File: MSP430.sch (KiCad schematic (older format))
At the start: 23 parts, among them P1 CONN_02X07, SW1 2M1-SP1-T2-B4-M6RE, U6 MSP430F2274TRHAR

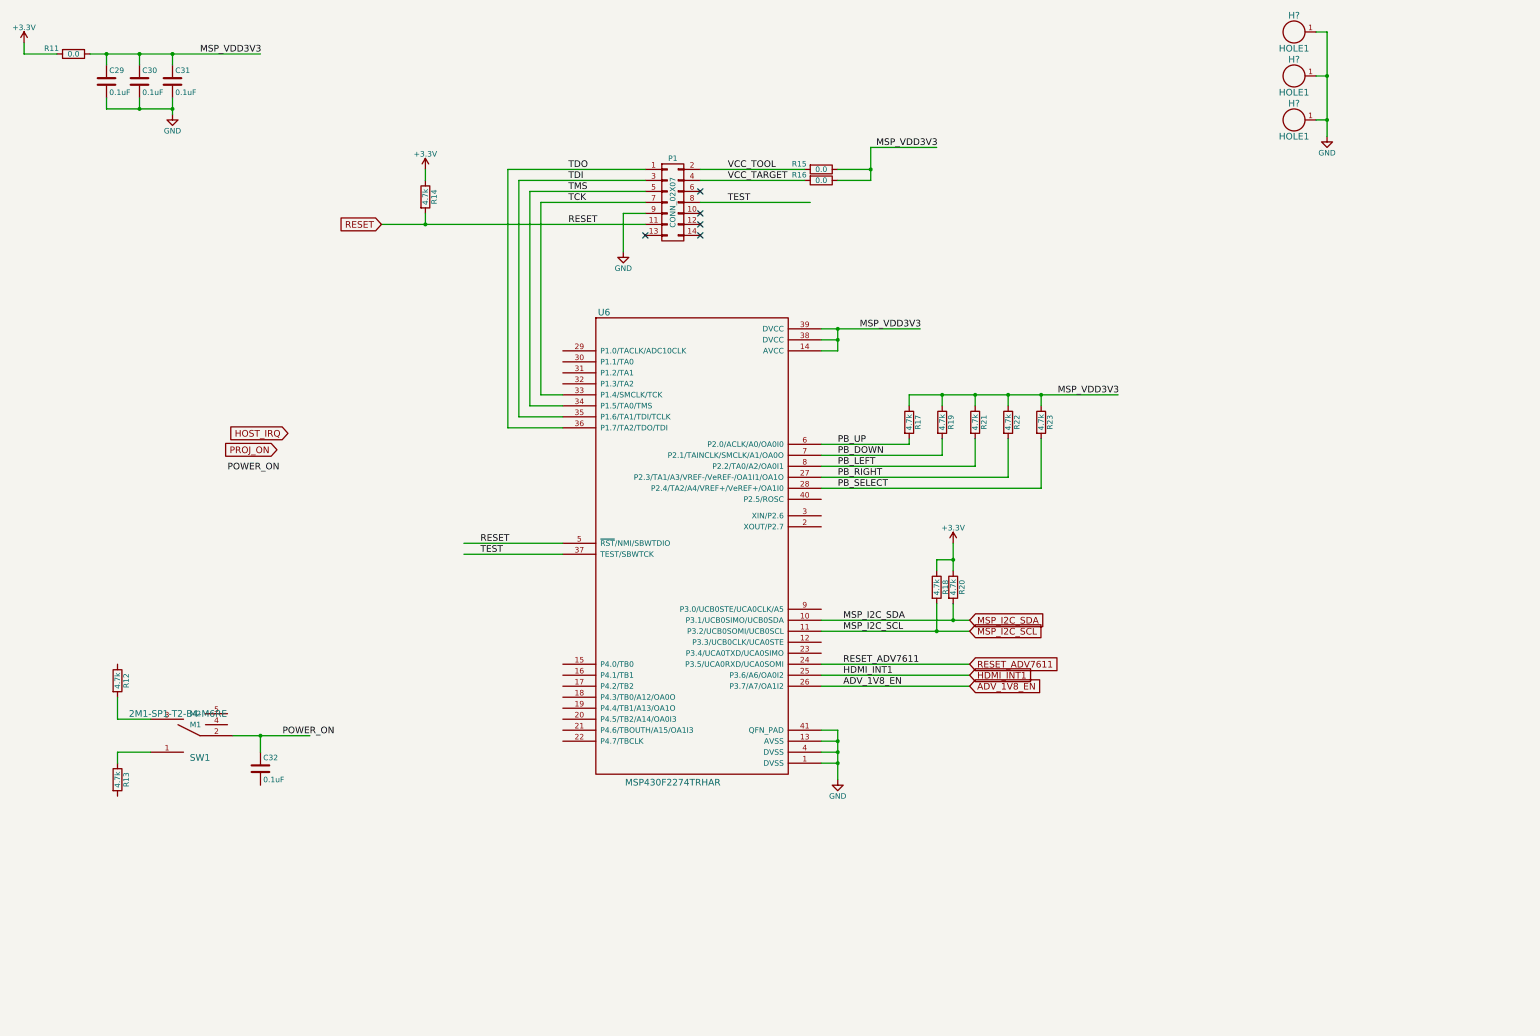
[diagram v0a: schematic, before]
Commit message: Hdmi and RGB is routed, waiting for trace matching
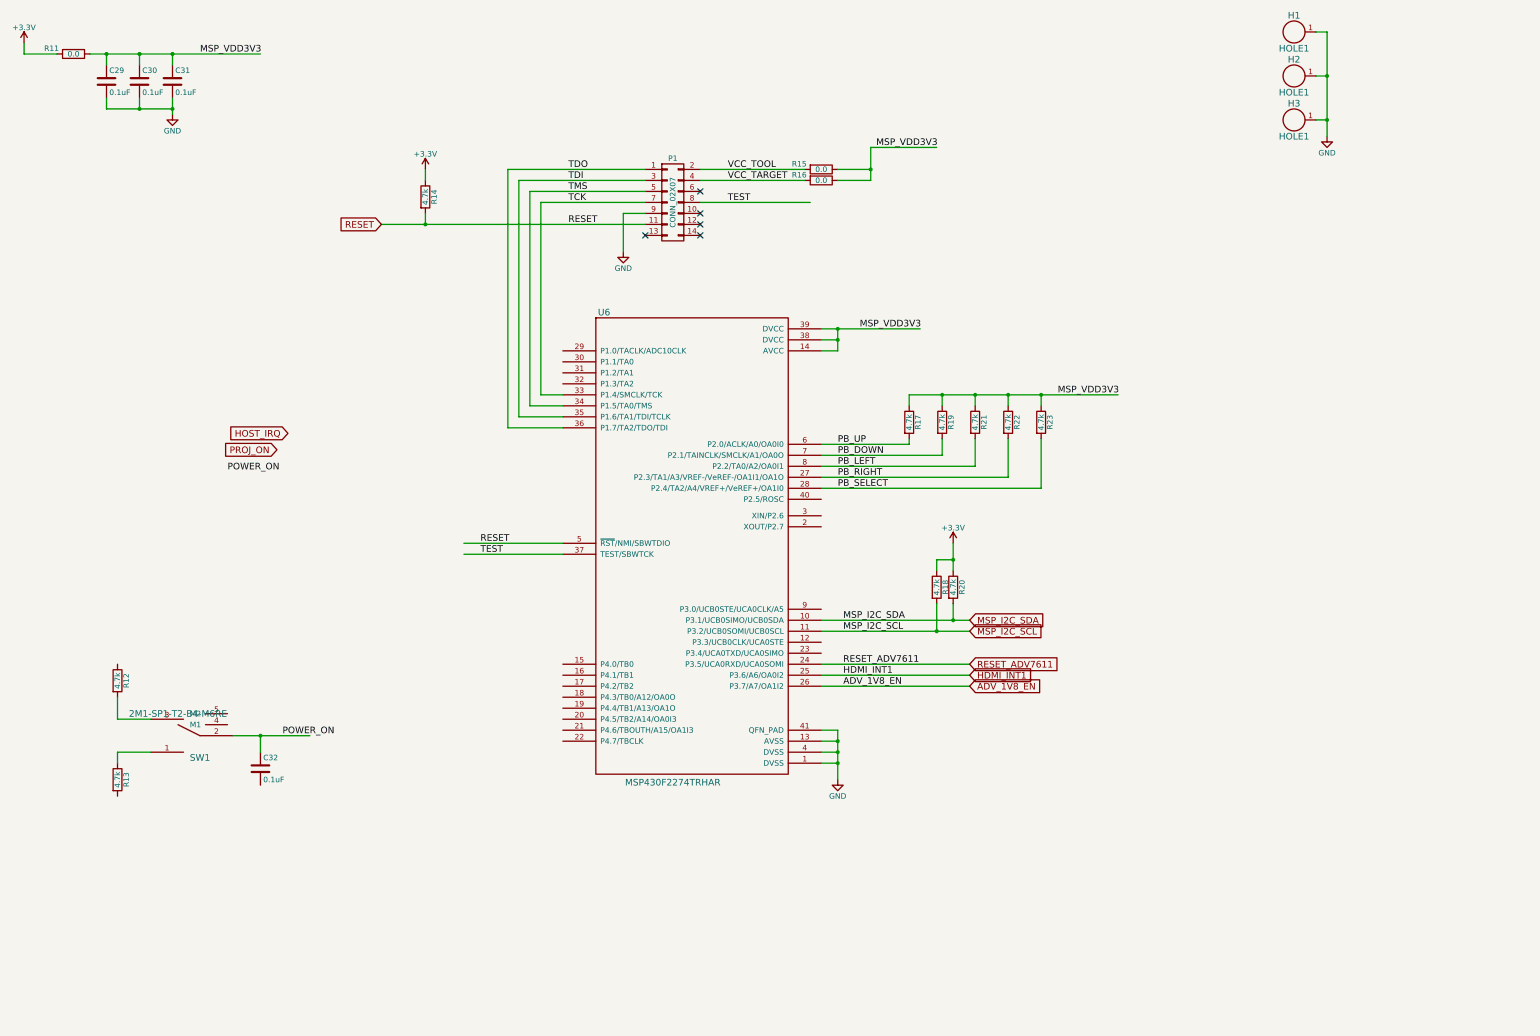
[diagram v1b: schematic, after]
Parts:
- H1, H2, H3: renamed from H?; footprint (none) -> Mounting_Holes:MountingHole_4.3mm_M4_Pad
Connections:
- wire segments 104 -> 81
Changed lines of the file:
@@
 $EndComp
 Wire Wire Line
-	4350 2750 4750 2750
-Wire Wire Line
-	4750 2750 6750 2750
+	4350 2750 6750 2750
 Wire Wire Line
 	4750 2750 4750 2650
@@
 	8500 2250 8800 2250
 Wire Wire Line
-	8800 2050 8800 2250
-Wire Wire Line
-	8800 2250 8800 2350
+	8800 2050 8800 2350
 Wire Wire Line
 	8800 2350 8500 2350
@@
 TEST
 Wire Wire Line
-	8350 6350 9550 6350
-Wire Wire Line
-	9550 6350 9700 6350
-Wire Wire Line
-	8350 6450 9400 6450
-Wire Wire Line
-	9400 6450 9700 6450
+	8350 6350 9700 6350
+Wire Wire Line
+	8350 6450 9700 6450
 $Comp
 L R R20
@@
 	9400 5800 9550 5800
 Wire Wire Line
-	9550 5650 9550 5800
-Wire Wire Line
-	9550 5800 9550 5900
+	9550 5650 9550 5900
 Connection ~ 9550 5800
 Wire Wire Line
@@
 $EndComp
 Wire Wire Line
-	8500 7350 8500 7450
-Wire Wire Line
-	8500 7450 8500 7550
-Wire Wire Line
-	8500 7550 8500 7650
-Wire Wire Line
-	8500 7650 8500 7800
+	8500 7350 8500 7800
 Wire Wire Line
 	8500 7350 8350 7350
@@
 	1100 1200 1400 1200
 Wire Wire Line
-	1700 1200 1850 1200
-Wire Wire Line
-	1850 1200 2150 1200
-Wire Wire Line
-	2150 1200 2450 1200
-Wire Wire Line
-	2450 1200 3250 1200
+	1700 1200 3250 1200
 Wire Wire Line
 	2450 1200 2450 1300
@@
 $EndComp
 Wire Wire Line
-	2450 1600 2450 1700
-Wire Wire Line
-	2450 1700 2450 1750
-Wire Wire Line
-	1850 1700 2150 1700
-Wire Wire Line
-	2150 1700 2450 1700
+	2450 1600 2450 1750
+Wire Wire Line
+	1850 1700 2450 1700
 Connection ~ 2450 1700
 Wire Wire Line
@@
 MSP_VDD3V3
 Wire Wire Line
-	8350 3700 8500 3700
-Wire Wire Line
-	8500 3700 9250 3700
+	8350 3700 9250 3700
 Wire Wire Line
 	8350 3800 8500 3800
 Wire Wire Line
-	8500 3700 8500 3800
-Wire Wire Line
-	8500 3800 8500 3900
+	8500 3700 8500 3900
 Connection ~ 8500 3700
 Wire Wire Line
@@
 MSP_VDD3V3
 Wire Wire Line
-	9150 4300 9450 4300
-Wire Wire Line
-	9450 4300 9750 4300
-Wire Wire Line
-	9750 4300 10050 4300
-Wire Wire Line
-	10050 4300 10350 4300
-Wire Wire Line
-	10350 4300 11050 4300
+	9150 4300 11050 4300
 Wire Wire Line
 	9150 4300 9150 4400
@@
 $EndComp
 Wire Wire Line
-	3000 7400 3250 7400
-Wire Wire Line
-	3250 7400 3700 7400
+	3000 7400 3700 7400
 Wire Wire Line
 	3250 7400 3250 7550
@@
 POWER_ON
 $Comp
-L HOLE1 H?
+L HOLE1 H1
 U 1 1 56F98079
 P 12650 1000
-F 0 "H?" H 12650 1150 60  0000 C CNN
+F 0 "H1" H 12650 1150 60  0000 C CNN
 F 1 "HOLE1" H 12650 850 60  0000 C CNN
-F 2 "" H 12650 1000 60  0000 C CNN
+F 2 "Mounting_Holes:MountingHole_4.3mm_M4_Pad" H 12650 1000 60  0001 C CNN
 F 3 "" H 12650 1000 60  0000 C CNN
 	1    12650 1000
@@
 $EndComp
 $Comp
-L HOLE1 H?
+L HOLE1 H2
 U 1 1 56F9810C
 P 12650 1400
-F 0 "H?" H 12650 1550 60  0000 C CNN
+F 0 "H2" H 12650 1550 60  0000 C CNN
 F 1 "HOLE1" H 12650 1250 60  0000 C CNN
-F 2 "" H 12650 1400 60  0000 C CNN
+F 2 "Mounting_Holes:MountingHole_4.3mm_M4_Pad" H 12650 1400 60  0001 C CNN
 F 3 "" H 12650 1400 60  0000 C CNN
 	1    12650 1400
@@
 $EndComp
 $Comp
-L HOLE1 H?
+L HOLE1 H3
 U 1 1 56F9815A
 P 12650 1800
-F 0 "H?" H 12650 1950 60  0000 C CNN
+F 0 "H3" H 12650 1950 60  0000 C CNN
 F 1 "HOLE1" H 12650 1650 60  0000 C CNN
-F 2 "" H 12650 1800 60  0000 C CNN
+F 2 "Mounting_Holes:MountingHole_4.3mm_M4_Pad" H 12650 1800 60  0001 C CNN
 F 3 "" H 12650 1800 60  0000 C CNN
 	1    12650 1800
@@
 	12850 1000 12950 1000
 Wire Wire Line
-	12950 1000 12950 1400
-Wire Wire Line
-	12950 1400 12950 1800
-Wire Wire Line
-	12950 1800 12950 1800
+	12950 1000 12950 1950
 Wire Wire Line
 	12950 1800 12850 1800
@@
 Connection ~ 12950 1400
 $Comp
-L GND #PWR?
+L GND #PWR049
 U 1 1 56F98389
 P 12950 1950
-F 0 "#PWR?" H 12950 1700 50  0001 C CNN
+F 0 "#PWR049" H 12950 1700 50  0001 C CNN
 F 1 "GND" H 12950 1800 50  0000 C CNN
 F 2 "" H 12950 1950 60  0000 C CNN
@@
 	1    0    0    -1
 $EndComp
-Wire Wire Line
-	12950 1950 12950 1800
 Connection ~ 12950 1800
 $EndSCHEMATC

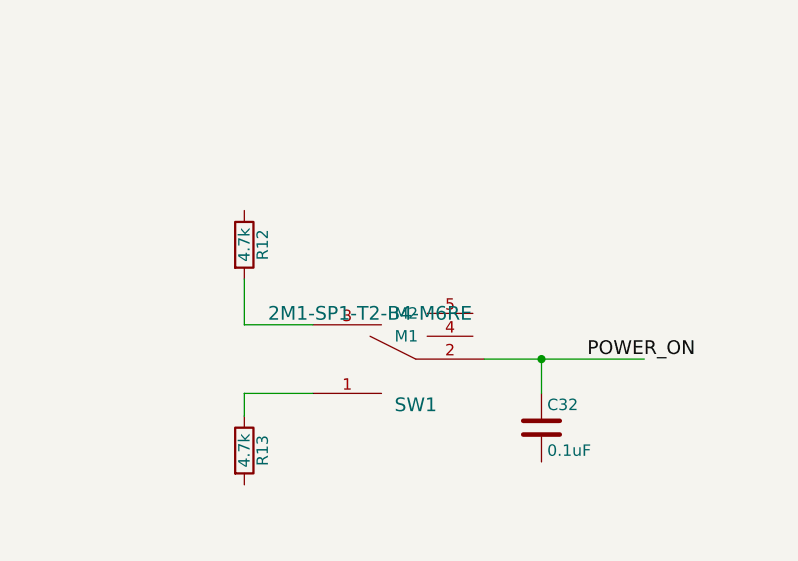
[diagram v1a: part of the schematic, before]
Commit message: Basic layout of all components on PCB
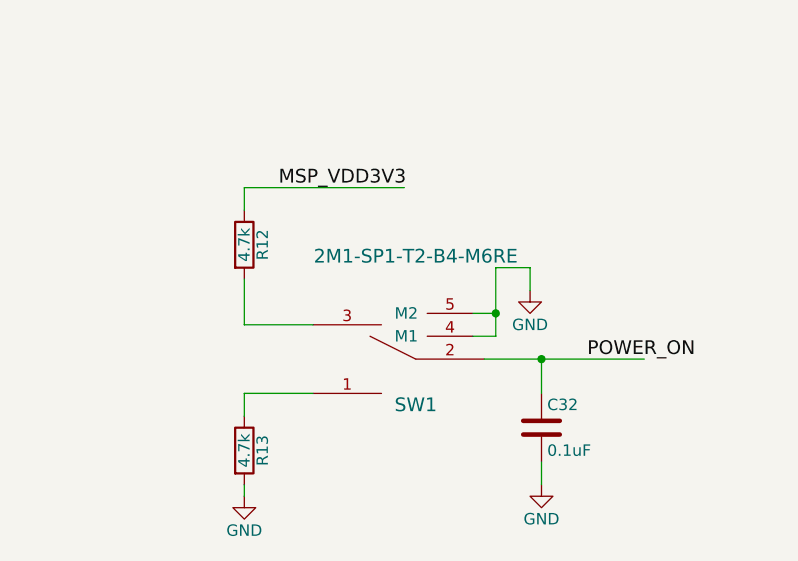
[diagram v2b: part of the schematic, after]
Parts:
- SW1: footprint (none) -> misc:2M1-SP1-T2-B4-M6RE
- U6: footprint (none) -> Housings_DFN_QFN:QFN-40-1EP_6x6mm_Pitch0.5mm
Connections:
- wire segments 81 -> 90
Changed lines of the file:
@@
 F 0 "U6" H 6375 3650 60  0000 C CNN
 F 1 "MSP430F2274TRHAR" H 7000 -625 60  0000 C CNN
-F 2 "" H 6300 3600 60  0001 C CNN
+F 2 "Housings_DFN_QFN:QFN-40-1EP_6x6mm_Pitch0.5mm" H 6300 3600 60  0001 C CNN
 F 3 "" H 6300 3600 60  0000 C CNN
 	1    6300 3600
@@
 P 2550 7400
 F 0 "SW1" H 2400 7600 60  0000 C CNN
-F 1 "2M1-SP1-T2-B4-M6RE" H 2600 7200 60  0000 C CNN
-F 2 "" H 2600 7400 60  0001 C CNN
+F 1 "2M1-SP1-T2-B4-M6RE" H 2400 6950 60  0000 C CNN
+F 2 "misc:2M1-SP1-T2-B4-M6RE" H 2600 7400 60  0001 C CNN
 F 3 "" H 2600 7400 60  0000 C CNN
 F 4 "2M1-SP1-T2-B4-M6RE" H 2500 7700 60  0001 C CNN "Part #"
@@
 $EndComp
 Connection ~ 12950 1800
+$Comp
+L GND #PWR050
+U 1 1 56FB8AA9
+P 1950 8000
+F 0 "#PWR050" H 1950 7750 50  0001 C CNN
+F 1 "GND" H 1950 7850 50  0000 C CNN
+F 2 "" H 1950 8000 60  0000 C CNN
+F 3 "" H 1950 8000 60  0000 C CNN
+	1    1950 8000
+	1    0    0    -1
+$EndComp
+$Comp
+L GND #PWR051
+U 1 1 56FB8B83
+P 3250 7950
+F 0 "#PWR051" H 3250 7700 50  0001 C CNN
+F 1 "GND" H 3250 7800 50  0000 C CNN
+F 2 "" H 3250 7950 60  0000 C CNN
+F 3 "" H 3250 7950 60  0000 C CNN
+	1    3250 7950
+	1    0    0    -1
+$EndComp
+Wire Wire Line
+	3250 7950 3250 7850
+Wire Wire Line
+	1950 8000 1950 7950
+Text Label 2100 6650 0    60   ~ 0
+MSP_VDD3V3
+Wire Wire Line
+	1950 6750 1950 6650
+Wire Wire Line
+	1950 6650 2650 6650
+$Comp
+L GND #PWR052
+U 1 1 56FB955B
+P 3200 7100
+F 0 "#PWR052" H 3200 6850 50  0001 C CNN
+F 1 "GND" H 3200 6950 50  0000 C CNN
+F 2 "" H 3200 7100 60  0000 C CNN
+F 3 "" H 3200 7100 60  0000 C CNN
+	1    3200 7100
+	1    0    0    -1
+$EndComp
+Wire Wire Line
+	2950 7300 3050 7300
+Wire Wire Line
+	3050 7300 3050 7000
+Wire Wire Line
+	3050 7000 3200 7000
+Wire Wire Line
+	3200 7000 3200 7100
+Wire Wire Line
+	2950 7200 3050 7200
+Connection ~ 3050 7200
 $EndSCHEMATC

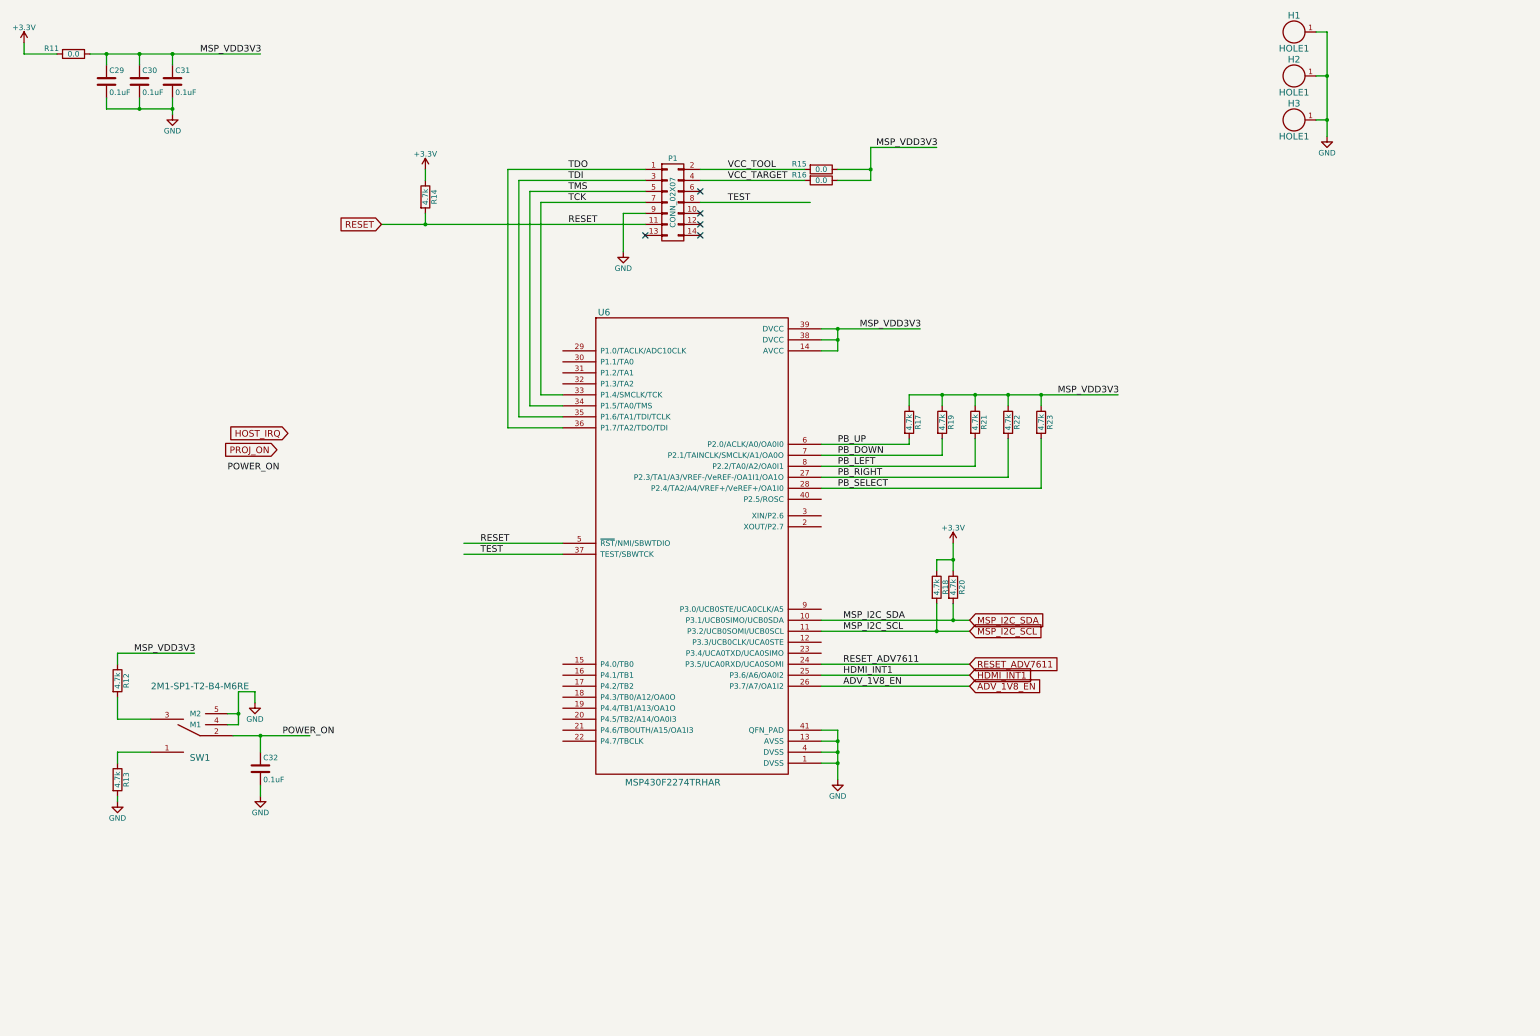
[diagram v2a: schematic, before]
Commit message: Routing power, changed buttons connections, and a few pther connections
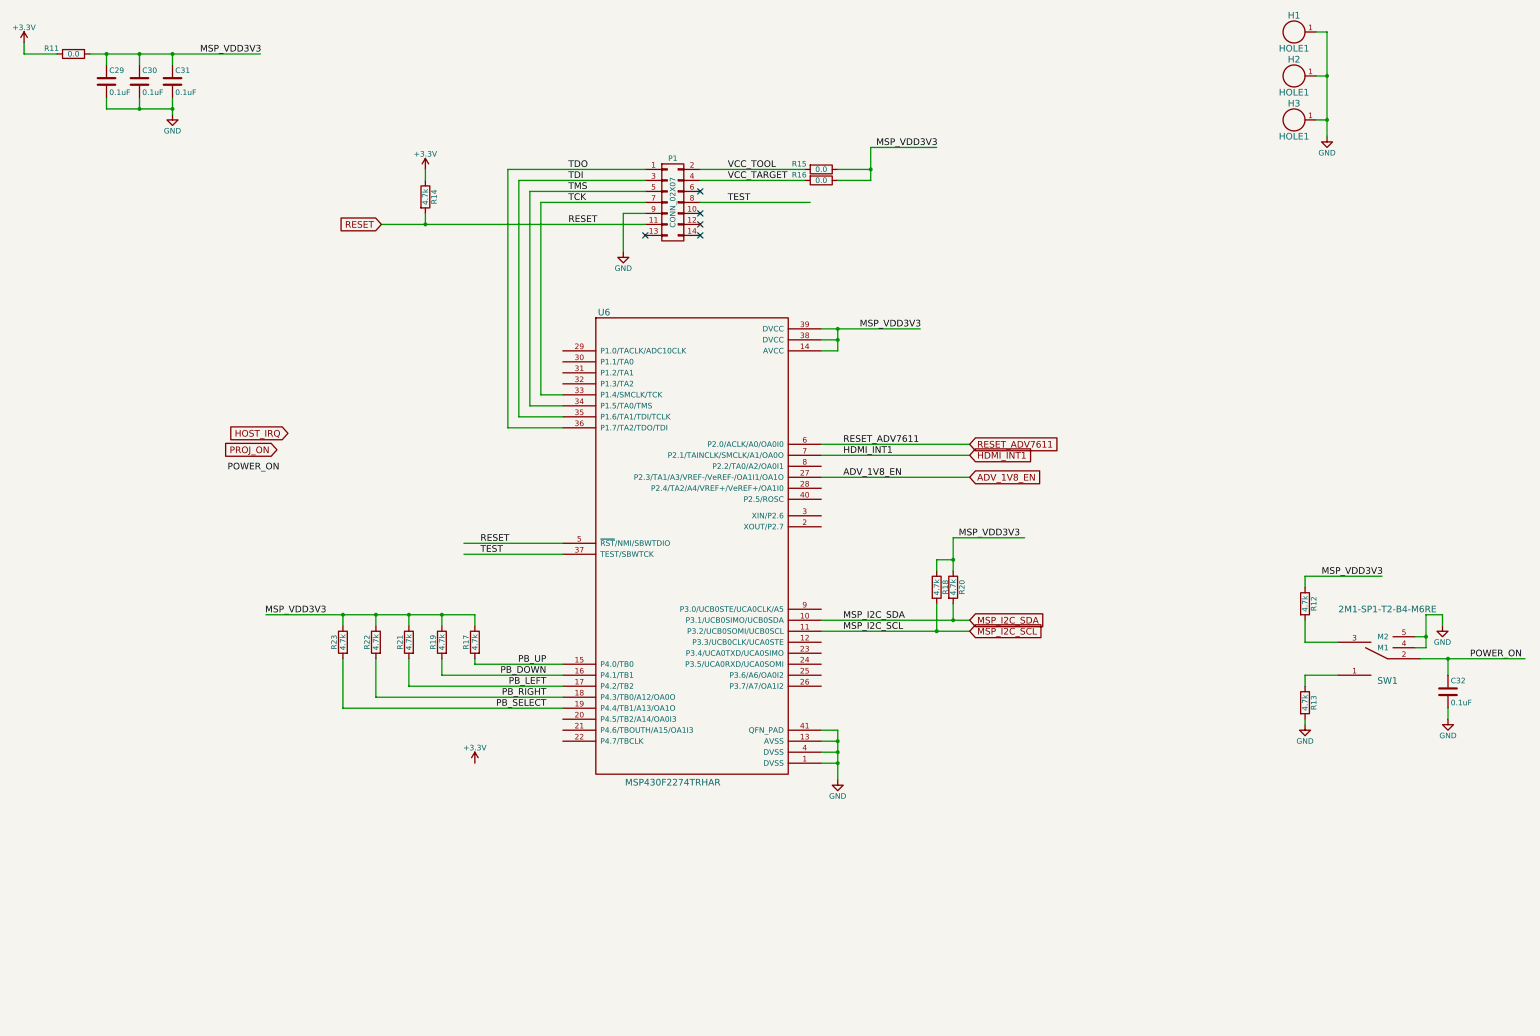
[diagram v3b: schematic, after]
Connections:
- wire segments 90 -> 91
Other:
- moved on the sheet: C32, R12, R13, R17, R19, R21, R22, R23, SW1

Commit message: First Final -- Waiting for Checker
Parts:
- added D5, D6: LED, Capacitors_SMD:C_0603, symbol LED
- added P3: CONN_01X06, Pin_Headers:Pin_Header_Straight_1x06, symbol CONN_01X06
- added R31, R34: 270, Resistors_SMD:R_0402, symbol R
- added U12, U13: SN74AUP1G06DCKR, TO_SOT_Packages_SMD:SC-70-5, symbol SN74AUP1G06DCKR
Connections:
- net labels added: +3V3, DEBUG1, DEBUG1_DRIVE, DEBUG1_LED, DEBUG2, DEBUG2_DRIVE, DEBUG2_LED
- wire segments 91 -> 113
- no-connect marks 5 -> 18
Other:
- moved on the sheet: C32, R12, R13, R17, R18, R19, R20, R21, R22, R23, SW1
